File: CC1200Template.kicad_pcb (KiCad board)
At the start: 2 copper layers, 39.8 x 31.7 mm, 39 parts, among them J1 Conn_Coaxial, J3002 RFShield_OnePiece, U1 CC1200, Y2 40 MHz

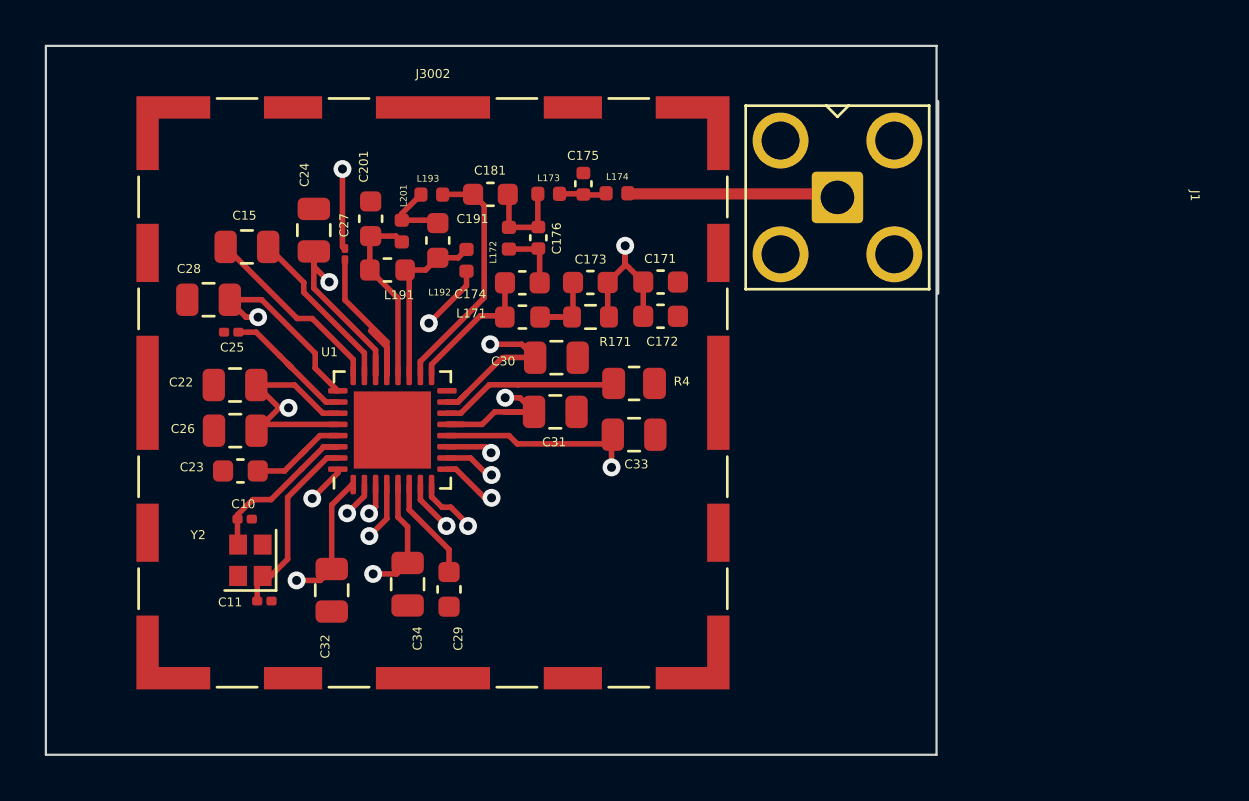
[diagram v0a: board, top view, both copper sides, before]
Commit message: fix clearance issues & errors in footprints
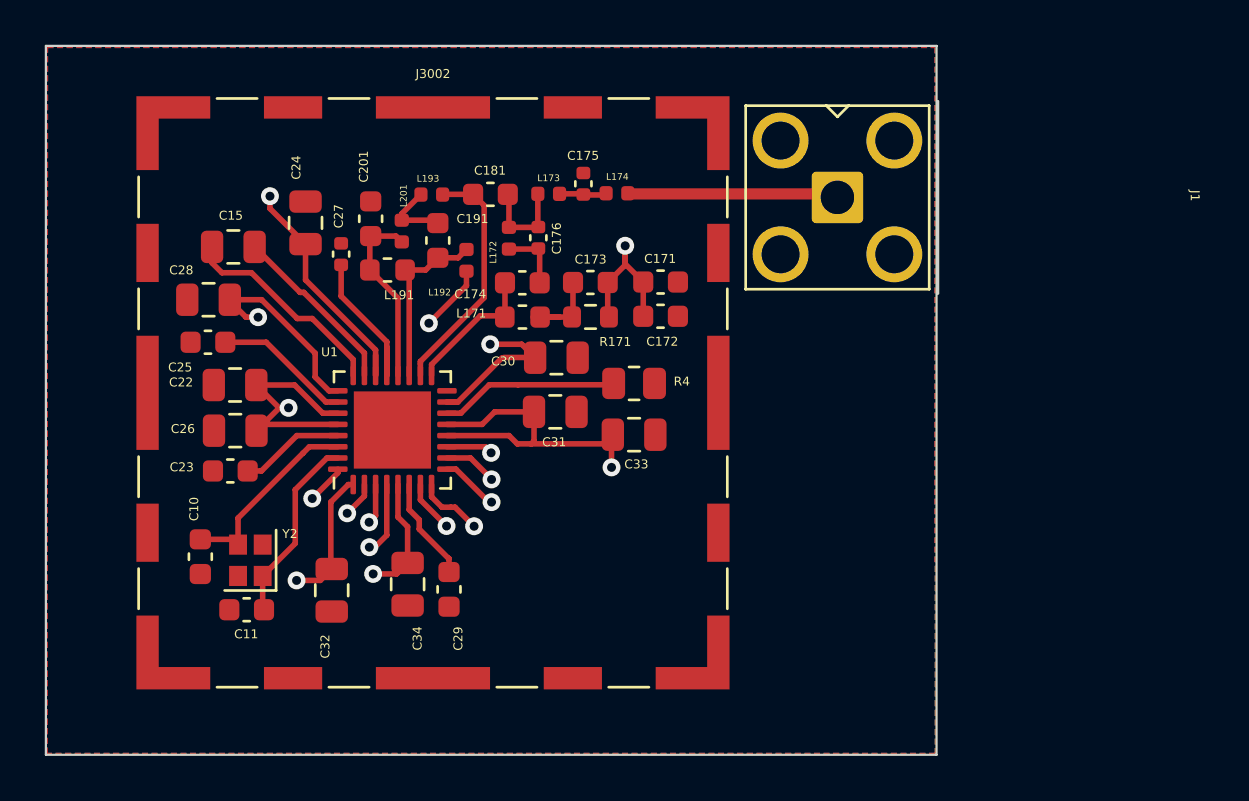
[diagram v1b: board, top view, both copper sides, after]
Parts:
- C10, C11, C25: footprint Capacitor_SMD:C_0201_0603Metric -> Capacitor_SMD:C_0603_1608Metric
- C27: footprint Capacitor_SMD:C_01005_0402Metric -> Capacitor_SMD:C_0402_1005Metric
- moved C10 2.60 mm to (87.1, 63.2), turned to 90 degrees
- moved C25 1.13 mm to (87.4, 53.6)
- moved C11 0.88 mm to (89.1, 65.5), turned to 180 degrees
- moved C15 0.60 mm to (88.5, 49.3)
- moved C24 0.49 mm to (91.8, 48.3)
- moved C23 0.45 mm to (88.4, 59.3)
- moved C27 0.17 mm to (93.4, 49.7)
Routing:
- net GND: track 8.41 -> 4.80 mm, vias 3 -> 2
- net +3V3: track 73.5 -> 72.2 mm, vias 9 -> 8
- net Net-(C27-Pad1): track 8.22 -> 7.06 mm
- net Net-(C15-Pad2): track 8.57 -> 9.52 mm
- net Net-(C10-Pad2): track 7.71 -> 8.41 mm
- net CC_1_GPIO2: track 2.63 -> 3.26 mm
- added copper zone on B.Cu, net +3V3
- added copper zone on F.Cu, net +3V3
- added copper zone on In1.Cu, net +3V3
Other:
- copper layers 2 -> 4

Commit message: fix clearance issues & errors in footprints and add vias for ground and add ground and vcc pours
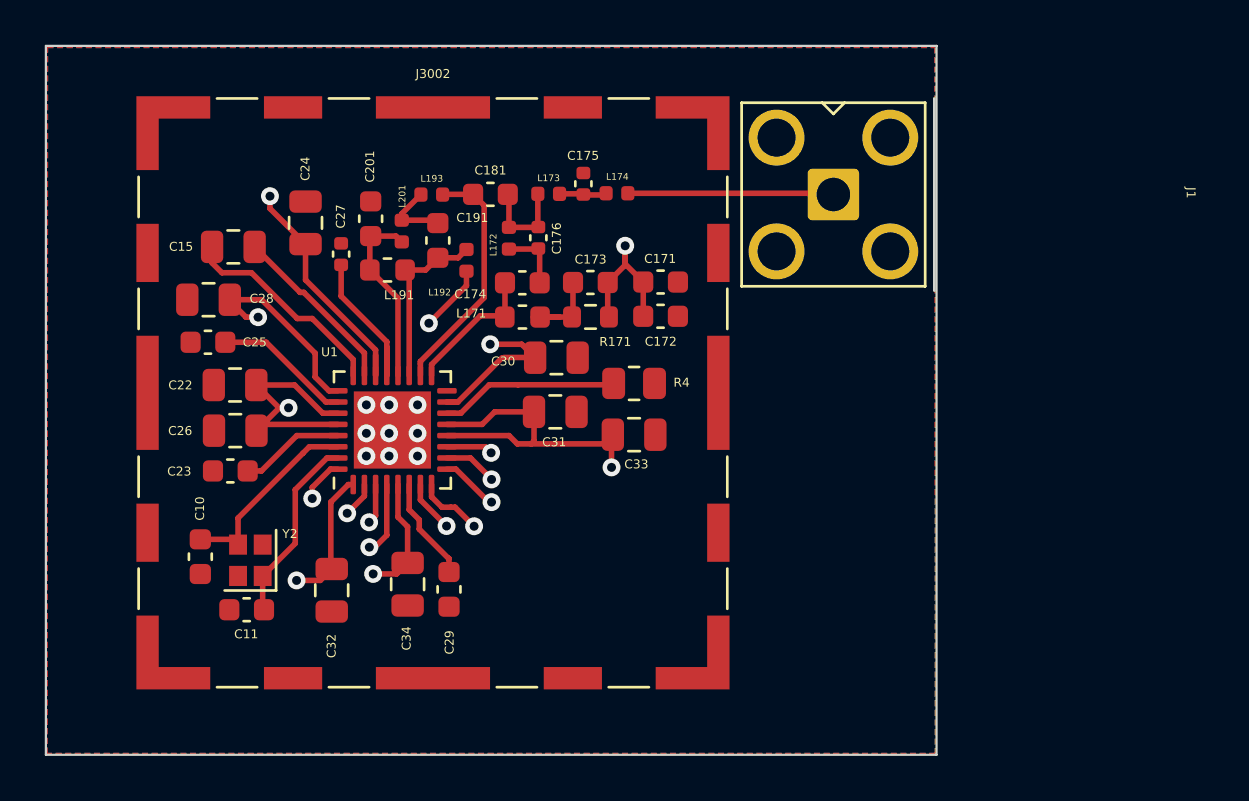
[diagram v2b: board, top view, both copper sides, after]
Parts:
- moved J1 0.22 mm to (130.8, 46.9)
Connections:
- J3002 pad 1: unconnected-(J3002-Pad1) -> GND
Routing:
- net GND: track 4.80 -> 5.00 mm, vias 2 -> 11
- added copper zone on F.Cu, net GND
- added copper zone on In1.Cu, net GND
- removed copper zone on F.Cu, net +3V3
- removed copper zone on In1.Cu, net +3V3
